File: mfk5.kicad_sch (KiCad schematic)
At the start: 12 parts, among them SW1 RST, SW2 COL1_ROW1, SW3 COL2_ROW1, SW4 COL1_ROW2, SW5 COL2_ROW2, SW6 COL1_ROW3, U1 Pro Micro

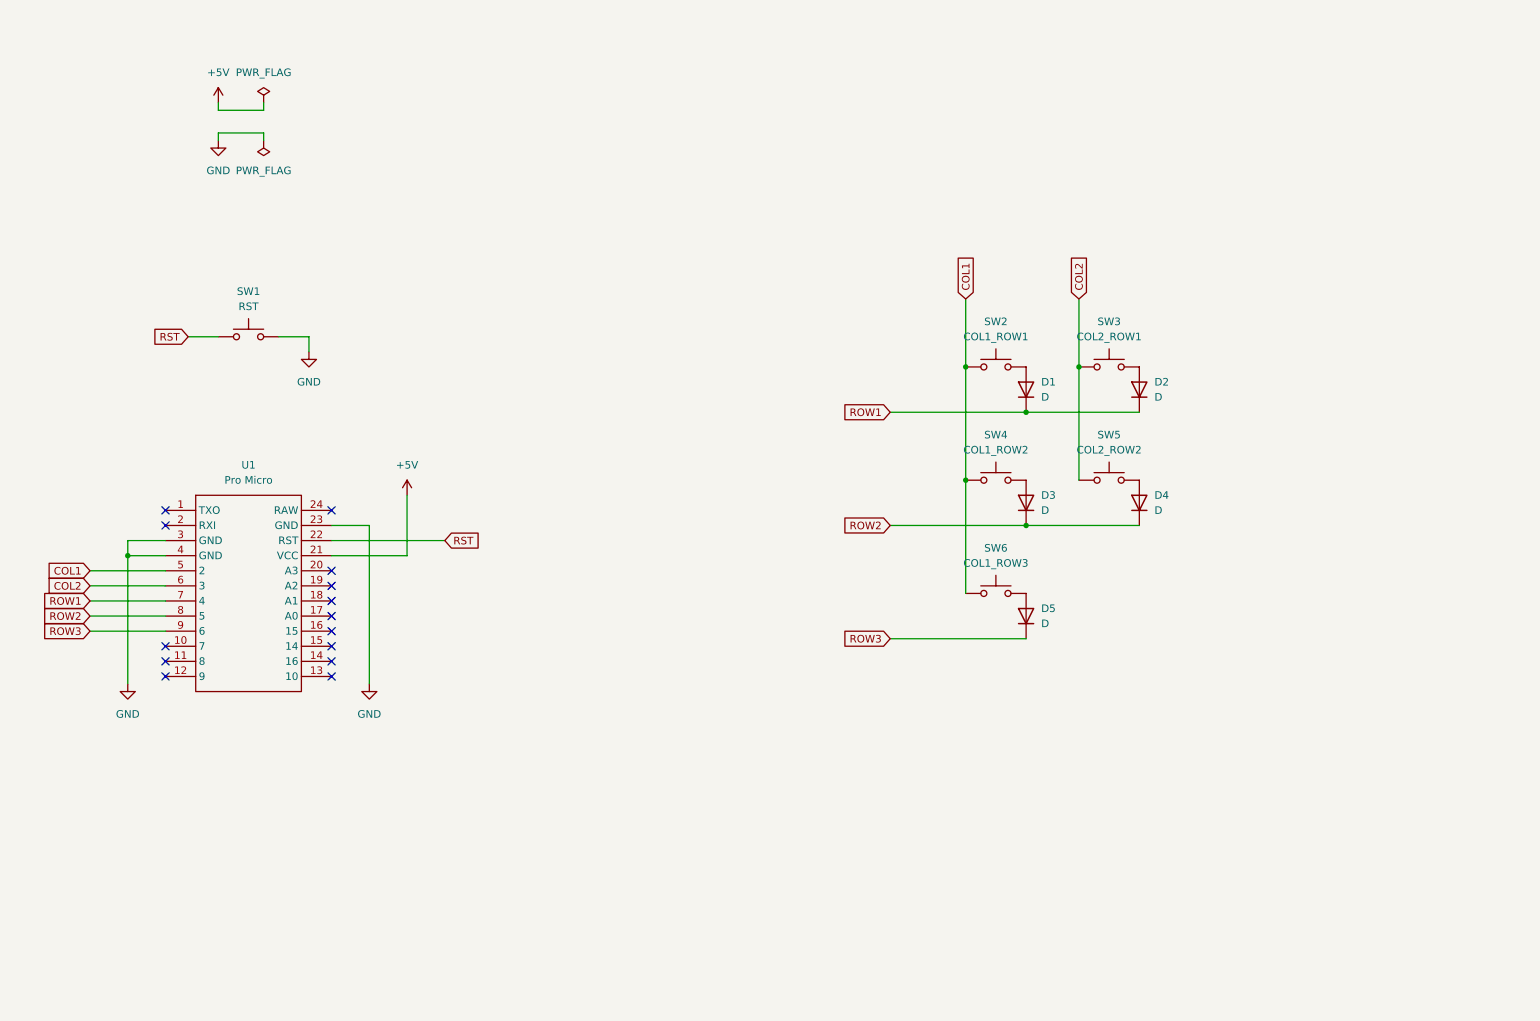
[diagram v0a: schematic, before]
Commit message: Add ATmega32u4 and related components.
Stop using Pro Micro, going to use PCBA to SMT components.
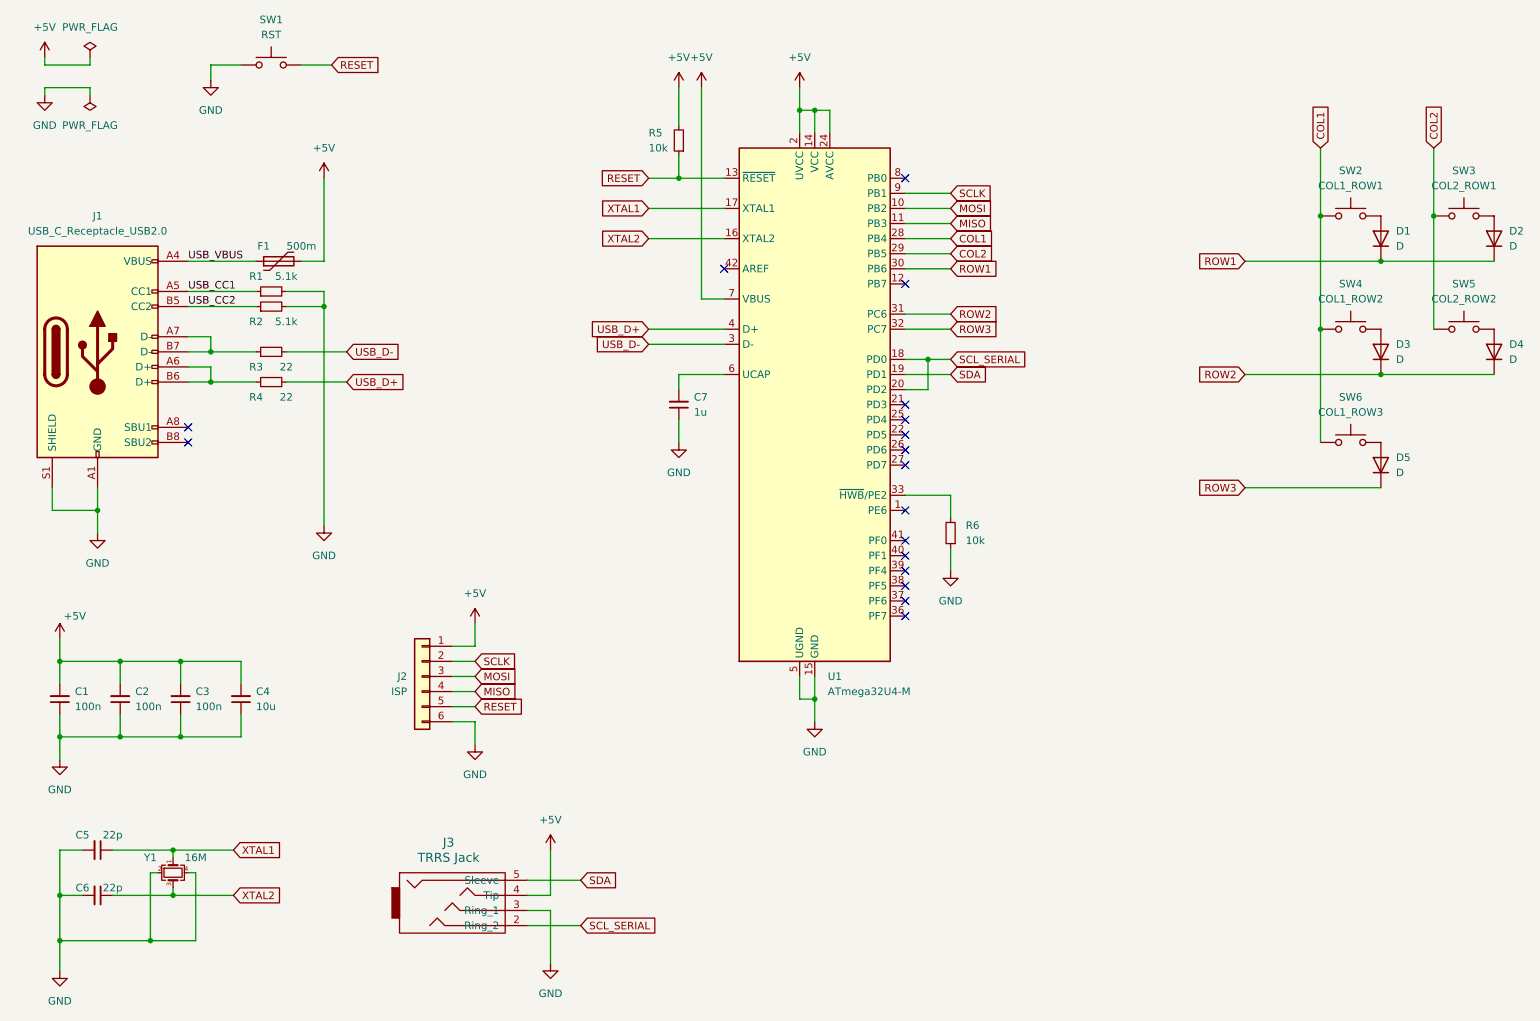
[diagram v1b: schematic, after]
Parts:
- removed U1: Pro Micro, Pro_Micro:Pro_Micro, symbol Pro_Micro:Pro_Micro
- added C1, C2, C3: 100n, Capacitor_SMD:C_0805_2012Metric_Pad1.18x1.45mm_HandSolder, symbol Device:C_Small
- added C4: 10u, Capacitor_SMD:C_0805_2012Metric_Pad1.18x1.45mm_HandSolder, symbol Device:C_Small
- added C5, C6: 22p, Capacitor_SMD:C_0805_2012Metric_Pad1.18x1.45mm_HandSolder, symbol Device:C_Small
- added C7: 1u, Capacitor_SMD:C_0805_2012Metric_Pad1.18x1.45mm_HandSolder, symbol Device:C_Small
- added F1: 500m, Fuse:Fuse_1206_3216Metric_Pad1.42x1.75mm_HandSolder, symbol Device:Polyfuse
- added J1: USB_C_Receptacle_USB2.0, Connector_USB:USB_C_Receptacle_HRO_TYPE-C-31-M-12, symbol Connector:USB_C_Receptacle_USB2.0
- added J2: ISP, Connector_PinHeader_2.54mm:PinHeader_1x06_P2.54mm_Vertical, symbol Connector_Generic:Conn_01x06
- added J3: TRRS Jack, Connector_Additions:TRRS_Jack_3.5mm_PJ320A, symbol Connector_Additions:TRRS_Jack
- added R1, R2: 5.1k, Resistor_SMD:R_0805_2012Metric_Pad1.20x1.40mm_HandSolder, symbol Device:R_Small
- added R3, R4: 22, Resistor_SMD:R_0805_2012Metric_Pad1.20x1.40mm_HandSolder, symbol Device:R_Small
- added R5, R6: 10k, Resistor_SMD:R_0805_2012Metric_Pad1.20x1.40mm_HandSolder, symbol Device:R_Small
- added U1: ATmega32U4-M, Package_DFN_QFN:QFN-44-1EP_7x7mm_P0.5mm_EP5.2x5.2mm, symbol MCU_Microchip_ATmega:ATmega32U4-M
- added Y1: 16M, Crystal:Crystal_SMD_3225-4Pin_3.2x2.5mm_HandSoldering, symbol Device:Crystal_GND24_Small
- D1, D2, D3, D4, D5: LCSC (none) -> C81598
- SW1: footprint Button_Switch_THT:SW_PUSH_6mm -> Button_Switch_Additions:SW_Push_3.5x6mm_THT
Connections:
- net +5V: now also C1.2, C2.2, C3.2, C4.2, F1.2, J2.1 (Pin_1), J3.4 (Tip), R5.2, U1.14 (VCC), U1.2 (UVCC), U1.24 (AVCC), U1.34 (VCC), U1.44 (AVCC), U1.7 (VBUS)
- net COL1: now also U1.28 (PB4)
- net COL2: now also U1.29 (PB5)
- net GND: now also C1.1, C2.1, C3.1, C4.1, C5.2, C6.2, C7.1, J1.A1 (GND), J1.A12 (GND), J1.B1 (GND), J1.B12 (GND), J1.S1 (SHIELD), J2.6 (Pin_6), J3.3 (Ring_1), R1.2, R2.2, R6.1, U1.15 (GND), U1.23 (GND), U1.35 (GND), U1.43 (GND), U1.45 (GND), U1.5 (UGND), Y1.2, Y1.4
- net ROW1: now also U1.30 (PB6)
- net ROW2: now also U1.31 (PC6)
- net ROW3: now also U1.32 (PC7)
- net RST renamed RESET
- net RESET: now also J2.5 (Pin_5), R5.1, U1.13 (~{RESET})
- new net: J1.A6 (D+), J1.B6 (D+), R4.1
- new net: J1.A7 (D-), J1.B7 (D-), R3.1
- new net: R6.2, U1.33 (~{HWB}/PE2)
- new net: C7.2, U1.6 (UCAP)
- new net MISO: J2.4 (Pin_4), U1.11 (PB3)
- new net MOSI: J2.3 (Pin_3), U1.10 (PB2)
- new net SCLK: J2.2 (Pin_2), U1.9 (PB1)
- new net SCL_SERIAL: J3.2 (Ring_2), U1.18 (PD0), U1.20 (PD2)
- new net SDA: J3.5 (Sleeve), U1.19 (PD1)
- new net USB_CC1: J1.A5 (CC1), R1.1
- new net USB_CC2: J1.B5 (CC2), R2.1
- new net USB_D+: R4.2, U1.4 (D+)
- new net USB_D-: R3.2, U1.3 (D-)
- new net USB_VBUS: F1.1, J1.A4 (VBUS), J1.A9 (VBUS), J1.B4 (VBUS), J1.B9 (VBUS)
- new net XTAL1: C5.1, U1.17 (XTAL1), Y1.1
- new net XTAL2: C6.1, U1.16 (XTAL2), Y1.3
- no-connect marks 14 -> 17
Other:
- moved on the sheet: D1, D2, D3, D4, D5, SW1, SW2, SW3, SW4, SW5, SW6
